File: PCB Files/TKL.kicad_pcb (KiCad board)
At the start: 2 copper layers, 350 x 123.8 mm, 557 parts, among them J1 USB_C, SW1 ESC, SW10 F9, SW100 RGUI_R2, SW101 RCTRL_R2, SW102 STEPPED_CAPS, SW103 RSHFT_175, SW104 Fn, SW105 BKSP_2U, SW11 F10, SW12 F11, SW13 F12, SW14 PRTSC, SW15 SCRLCK, SW16 PAUSE, SW17 GRV, SW18 1, SW19 2, SW2 F1, SW20 3, SW21 4, SW22 5, SW23 6, SW24 7, SW25 8, SW26 9, SW27 0, SW28 HIFEN, SW29 PLUS, SW3 F2, SW30 BCKSLSH, SW31 DEL, SW32 INS, SW33 HOME, SW34 PGUP, SW35 TAB, SW36 Q, SW37 W, SW38 E, SW39 R, SW4 F3, SW40 T, SW41 Y, SW42 U, SW43 I, SW44 O, SW45 P, SW46 LBRACES, SW47 RBRACES, SW48 BKSP_150, SW49 DEL, SW5 F4, SW50 END, SW51 PGDN, SW52 CAPS, SW53 A, SW54 S, SW55 D, SW56 F, SW57 G, SW58 H, SW59 J, SW6 F5, SW60 K, SW61 L, SW62 :, SW63 QUOTE, SW64 ENTER, SW65 LSHFT, SW66 Z, SW67 X, SW68 C, SW69 V, SW7 F6, SW70 B, SW71 N, SW72 M, SW73 <,, SW74 .>, SW75 /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

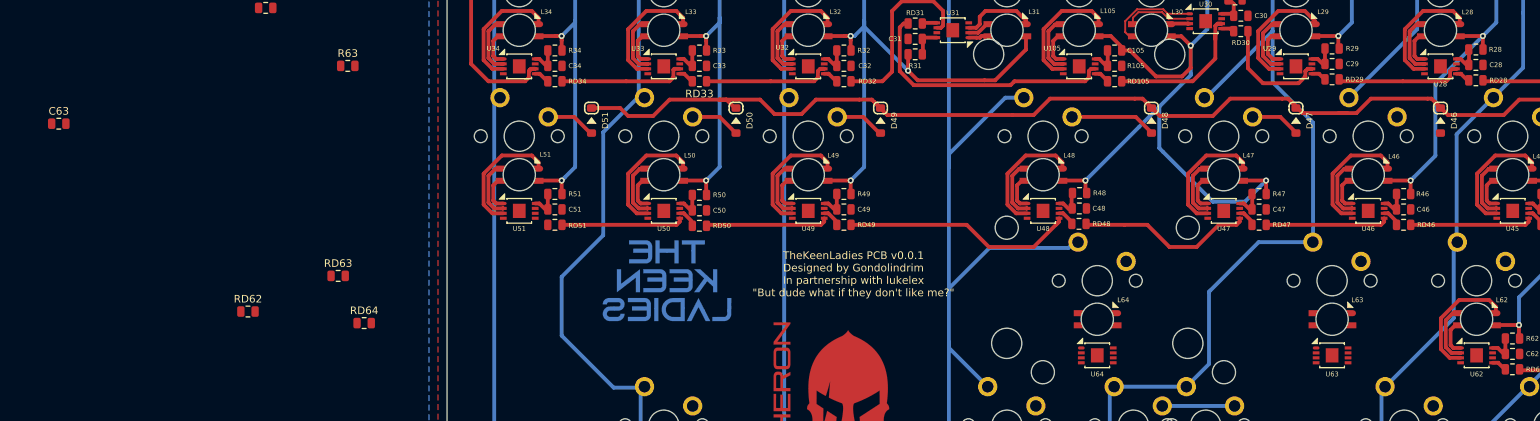
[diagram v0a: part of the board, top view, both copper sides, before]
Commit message: Routed SW63 RGB LED
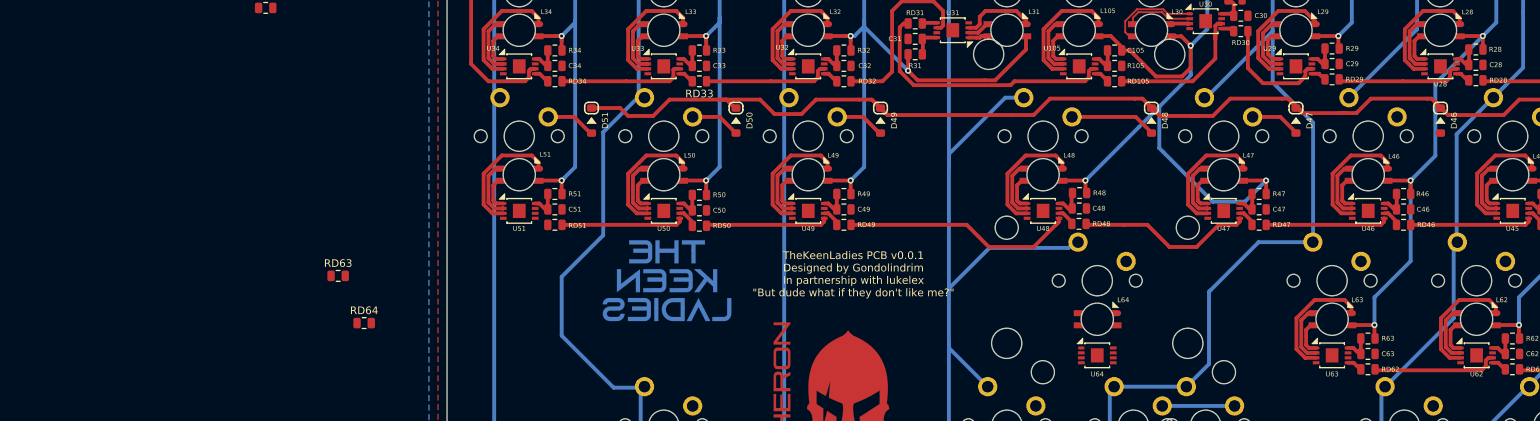
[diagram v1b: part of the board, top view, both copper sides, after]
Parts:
- moved C63 175.2 mm to (215.5, 122.8)
- moved RD62 147.8 mm to (215.5, 124.8), turned to 180 degrees
- moved R63 139.2 mm to (215.5, 120.7), turned to 180 degrees
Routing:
- net 5V: track 2172.4 -> 2198.1 mm, vias 66 -> 67
- net Net-(L63-Pad1): track 0.00 -> 16.6 mm
- net Net-(RD62-Pad1): track 0.00 -> 16.6 mm
- net Net-(L63-Pad2): track 0.00 -> 7.72 mm
- net Net-(L63-Pad3): track 0.00 -> 4.39 mm
- net Net-(C63-Pad1): track 0.00 -> 3.84 mm
- net Net-(RD62-Pad2): track 0.00 -> 1.97 mm

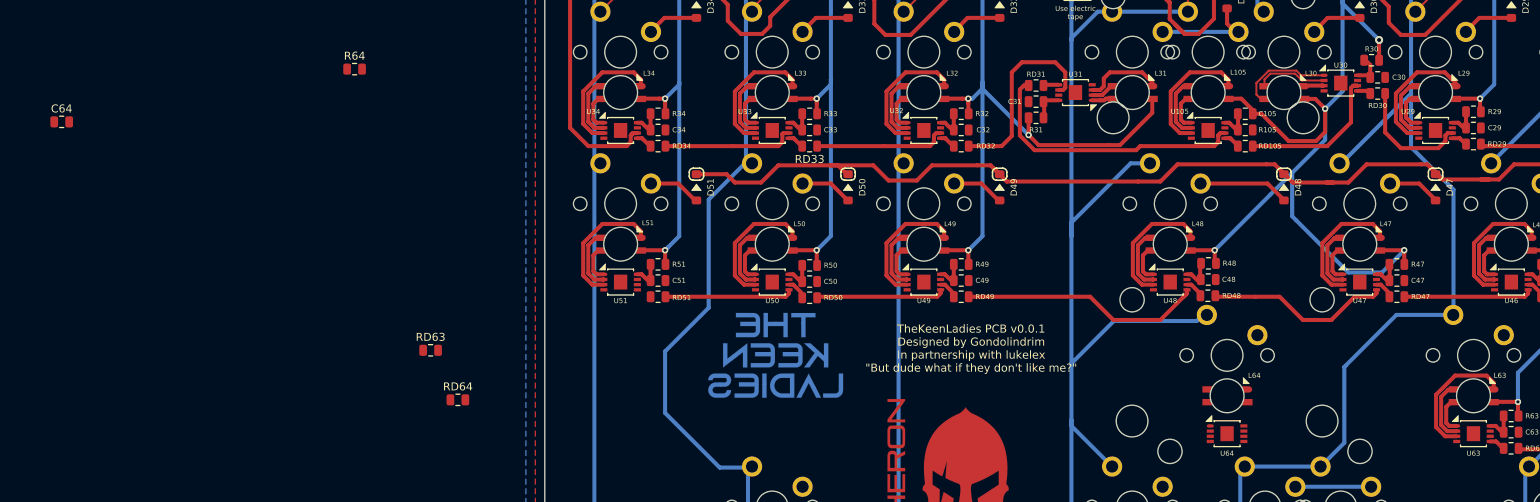
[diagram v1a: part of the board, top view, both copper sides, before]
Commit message: Routed SW64 RGB LED
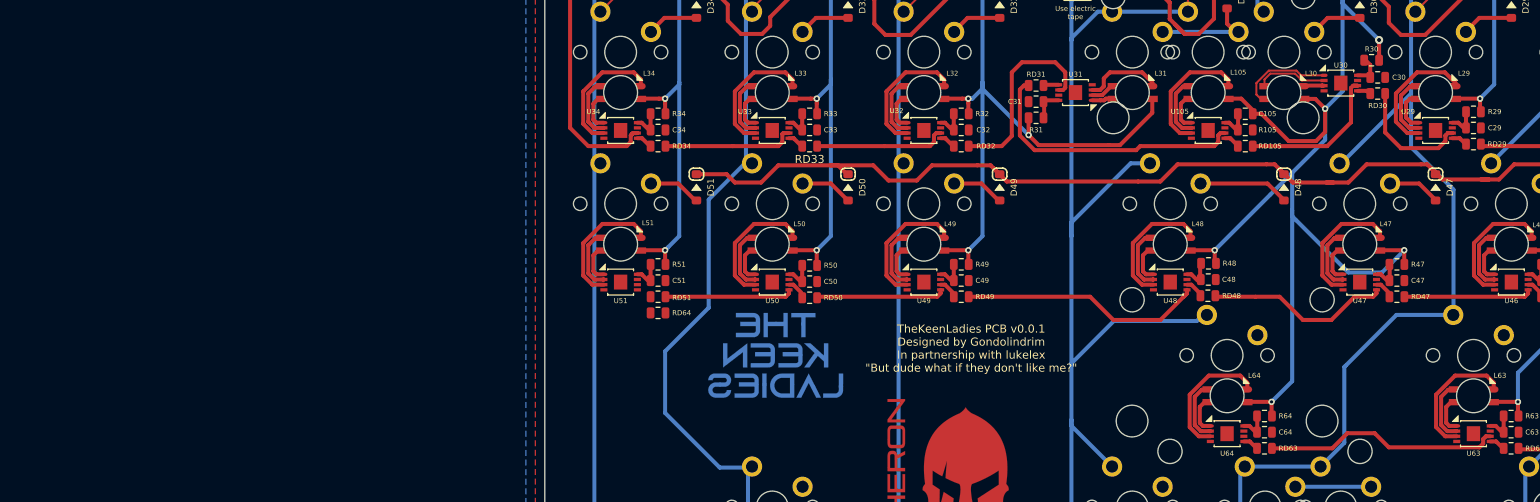
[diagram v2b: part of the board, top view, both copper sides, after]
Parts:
- moved C64 156.1 mm to (184.5, 122.8)
- moved R64 122.4 mm to (184.5, 120.7), turned to 180 degrees
- moved RD63 105.5 mm to (184.5, 124.8), turned to 180 degrees
- moved RD64 27.4 mm to (108.3, 107.8), turned to 180 degrees
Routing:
- net 5V: track 2198.1 -> 2228.0 mm, vias 67 -> 68
- net Net-(RD63-Pad1): track 0.00 -> 29.8 mm
- net Net-(L64-Pad1): track 0.00 -> 16.6 mm
- net Net-(L64-Pad2): track 0.00 -> 7.72 mm
- net Net-(L64-Pad3): track 0.00 -> 4.39 mm
- net Net-(C64-Pad1): track 0.00 -> 3.84 mm
- net Net-(RD63-Pad2): track 0.00 -> 1.97 mm

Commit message: Fix orientation of RD55, 56 and 57
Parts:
- turned RD55 to 180 degrees
- turned RD56 to 180 degrees
- turned RD57 to 180 degrees
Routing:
- net Net-(RD64-Pad1): track 0.00 -> 82.9 mm
- net Net-(RD54-Pad1): track 66.4 -> 16.6 mm
- net Net-(RD57-Pad1): track 0.00 -> 16.6 mm
- net Net-(RD56-Pad1): track 0.00 -> 16.6 mm
- net Net-(RD55-Pad1): track 0.00 -> 16.6 mm
- net Net-(RD54-Pad2): track 7.87 -> 1.97 mm
- net Net-(RD64-Pad2): track 0.00 -> 3.50 mm
- net Net-(RD57-Pad2): track 0.00 -> 1.97 mm
- net Net-(RD55-Pad2): track 0.00 -> 1.97 mm
- net Net-(RD56-Pad2): track 0.00 -> 1.97 mm
- net Net-(RD51-Pad1): track 0.00 -> 1.83 mm
